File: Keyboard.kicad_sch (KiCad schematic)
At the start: 0 parts

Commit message: Schematic checkpoint before I mess up the layout
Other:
- sheet Keypad_module ports: added K3V3, KCOM, KPRESENCE, KSCL, KSDA; removed 3V3, COM, PRESENCE, SCL, SDA
- sheet Main_board ports: added M3V3, MCOM, MPRESENCE, MSCL, MSDA; removed 3V3, COM, PRESENCE, SCL, SDA
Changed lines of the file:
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@@
 	(generator_version "9.0")
 	(paper "A4")
+	(wire
+		(pts
+			(xy 208.28 80.01) (xy 214.63 80.01)
+		)
+		(stroke
+			(width 0)
+			(type default)
+		)
+	)
+	(wire
+		(pts
+			(xy 208.28 90.17) (xy 214.63 90.17)
+		)
+		(stroke
+			(width 0)
+			(type default)
+		)
+	)
+	(wire
+		(pts
+			(xy 208.28 82.55) (xy 214.63 82.55)
+		)
+		(stroke
+			(width 0)
+			(type default)
+		)
+	)
+	(wire
+		(pts
+			(xy 208.28 87.63) (xy 214.63 87.63)
+		)
+		(stroke
+			(width 0)
+			(type default)
+		)
+	)
+	(wire
+		(pts
+			(xy 208.28 92.71) (xy 214.63 92.71)
+		)
+		(stroke
+			(width 0)
+			(type default)
+		)
+	)
+	(wire
+		(pts
+			(xy 208.28 85.09) (xy 214.63 85.09)
+		)
+		(stroke
+			(width 0)
+			(type default)
+		)
+	)
 	(sheet
 		(at 214.63 76.2)
@@
 			)
 		)
-		(pin "3V3" input
-			(at 214.63 80.01 180)
-			(effects
-				(font
-					(size 1.27 1.27)
-				)
-				(justify left)
-			)
-		)
-		(pin "COM" input
-			(at 214.63 87.63 180)
-			(effects
-				(font
-					(size 1.27 1.27)
-				)
-				(justify left)
-			)
-		)
 		(pin "GND" input
 			(at 214.63 82.55 180)
@@
 			)
 		)
-		(pin "PRESENCE" input
+		(pin "K3V3" input
+			(at 214.63 80.01 180)
+			(effects
+				(font
+					(size 1.27 1.27)
+				)
+				(justify left)
+			)
+		)
+		(pin "KCOM" input
+			(at 214.63 87.63 180)
+			(effects
+				(font
+					(size 1.27 1.27)
+				)
+				(justify left)
+			)
+		)
+		(pin "KPRESENCE" input
 			(at 214.63 85.09 180)
 			(effects
@@
 			)
 		)
-		(pin "SCL" input
+		(pin "KSCL" input
 			(at 214.63 92.71 180)
 			(effects
@@
 			)
 		)
-		(pin "SDA" input
+		(pin "KSDA" input
 			(at 214.63 90.17 180)
 			(effects
@@
 			)
 		)
-		(pin "3V3" input
-			(at 208.28 80.01 0)
-			(effects
-				(font
-					(size 1.27 1.27)
-				)
-				(justify right)
-			)
-		)
-		(pin "COM" input
-			(at 208.28 87.63 0)
-			(effects
-				(font
-					(size 1.27 1.27)
-				)
-				(justify right)
-			)
-		)
 		(pin "GND" input
 			(at 208.28 82.55 0)
@@
 			)
 		)
-		(pin "PRESENCE" input
+		(pin "M3V3" input
+			(at 208.28 80.01 0)
+			(effects
+				(font
+					(size 1.27 1.27)
+				)
+				(justify right)
+			)
+		)
+		(pin "MCOM" input
+			(at 208.28 87.63 0)
+			(effects
+				(font
+					(size 1.27 1.27)
+				)
+				(justify right)
+			)
+		)
+		(pin "MPRESENCE" input
 			(at 208.28 85.09 0)
 			(effects
@@
 			)
 		)
-		(pin "SCL" input
+		(pin "MSCL" input
 			(at 208.28 92.71 0)
 			(effects
@@
 			)
 		)
-		(pin "SDA" input
+		(pin "MSDA" input
 			(at 208.28 90.17 0)
 			(effects

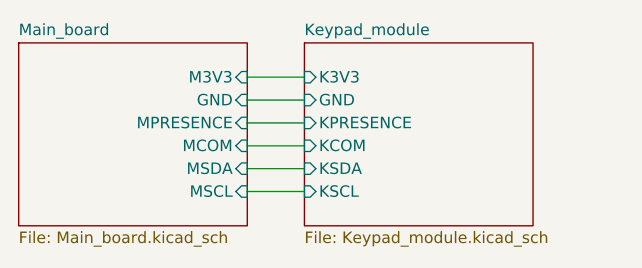
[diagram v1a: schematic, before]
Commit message: I gave up on the hotswao modularity thing
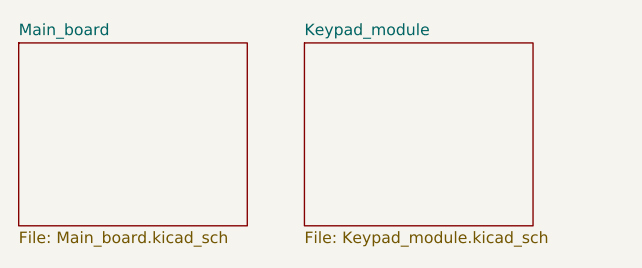
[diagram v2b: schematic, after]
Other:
- sheet Keypad_module ports: added none; removed GND, K3V3, KCOM, KPRESENCE, KSCL, KSDA
- sheet Main_board ports: added none; removed GND, M3V3, MCOM, MPRESENCE, MSCL, MSDA
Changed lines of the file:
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@@
 	(generator_version "9.0")
 	(paper "A4")
-	(wire
-		(pts
-			(xy 208.28 80.01) (xy 214.63 80.01)
-		)
-		(stroke
-			(width 0)
-			(type default)
-		)
-	)
-	(wire
-		(pts
-			(xy 208.28 90.17) (xy 214.63 90.17)
-		)
-		(stroke
-			(width 0)
-			(type default)
-		)
-	)
-	(wire
-		(pts
-			(xy 208.28 82.55) (xy 214.63 82.55)
-		)
-		(stroke
-			(width 0)
-			(type default)
-		)
-	)
-	(wire
-		(pts
-			(xy 208.28 87.63) (xy 214.63 87.63)
-		)
-		(stroke
-			(width 0)
-			(type default)
-		)
-	)
-	(wire
-		(pts
-			(xy 208.28 92.71) (xy 214.63 92.71)
-		)
-		(stroke
-			(width 0)
-			(type default)
-		)
-	)
-	(wire
-		(pts
-			(xy 208.28 85.09) (xy 214.63 85.09)
-		)
-		(stroke
-			(width 0)
-			(type default)
-		)
-	)
 	(sheet
 		(at 214.63 76.2)
@@
 				)
 				(justify left top)
-			)
-		)
-		(pin "GND" input
-			(at 214.63 82.55 180)
-			(effects
-				(font
-					(size 1.27 1.27)
-				)
-				(justify left)
-			)
-		)
-		(pin "K3V3" input
-			(at 214.63 80.01 180)
-			(effects
-				(font
-					(size 1.27 1.27)
-				)
-				(justify left)
-			)
-		)
-		(pin "KCOM" input
-			(at 214.63 87.63 180)
-			(effects
-				(font
-					(size 1.27 1.27)
-				)
-				(justify left)
-			)
-		)
-		(pin "KPRESENCE" input
-			(at 214.63 85.09 180)
-			(effects
-				(font
-					(size 1.27 1.27)
-				)
-				(justify left)
-			)
-		)
-		(pin "KSCL" input
-			(at 214.63 92.71 180)
-			(effects
-				(font
-					(size 1.27 1.27)
-				)
-				(justify left)
-			)
-		)
-		(pin "KSDA" input
-			(at 214.63 90.17 180)
-			(effects
-				(font
-					(size 1.27 1.27)
-				)
-				(justify left)
 			)
 		)
@@
 			)
 		)
-		(pin "GND" input
-			(at 208.28 82.55 0)
-			(effects
-				(font
-					(size 1.27 1.27)
-				)
-				(justify right)
-			)
-		)
-		(pin "M3V3" input
-			(at 208.28 80.01 0)
-			(effects
-				(font
-					(size 1.27 1.27)
-				)
-				(justify right)
-			)
-		)
-		(pin "MCOM" input
-			(at 208.28 87.63 0)
-			(effects
-				(font
-					(size 1.27 1.27)
-				)
-				(justify right)
-			)
-		)
-		(pin "MPRESENCE" input
-			(at 208.28 85.09 0)
-			(effects
-				(font
-					(size 1.27 1.27)
-				)
-				(justify right)
-			)
-		)
-		(pin "MSCL" input
-			(at 208.28 92.71 0)
-			(effects
-				(font
-					(size 1.27 1.27)
-				)
-				(justify right)
-			)
-		)
-		(pin "MSDA" input
-			(at 208.28 90.17 0)
-			(effects
-				(font
-					(size 1.27 1.27)
-				)
-				(justify right)
-			)
-		)
